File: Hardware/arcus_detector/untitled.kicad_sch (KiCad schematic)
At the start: 8 parts, among them J3 Arc_Input, U17 MAX11102AUB/V+, U4 MCP662-E/MF, U7 MCP6S91

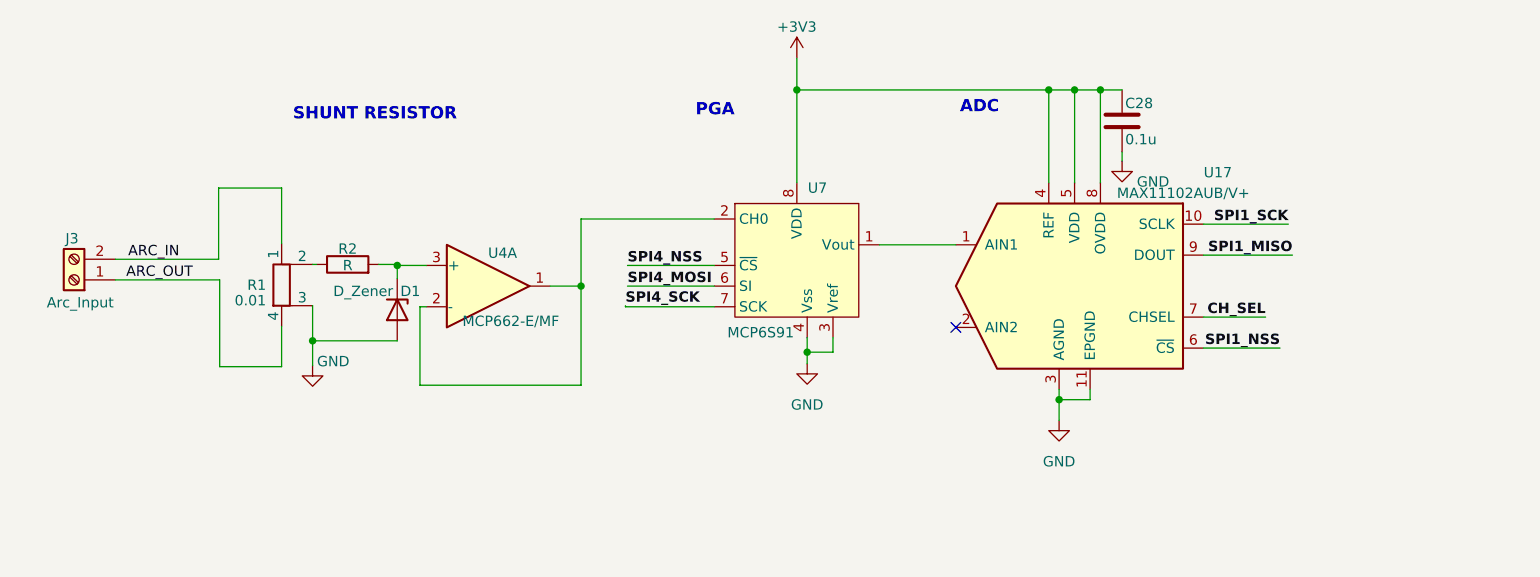
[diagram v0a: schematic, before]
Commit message: - complete sheme of prototype - PGA code works - treshold code added to main
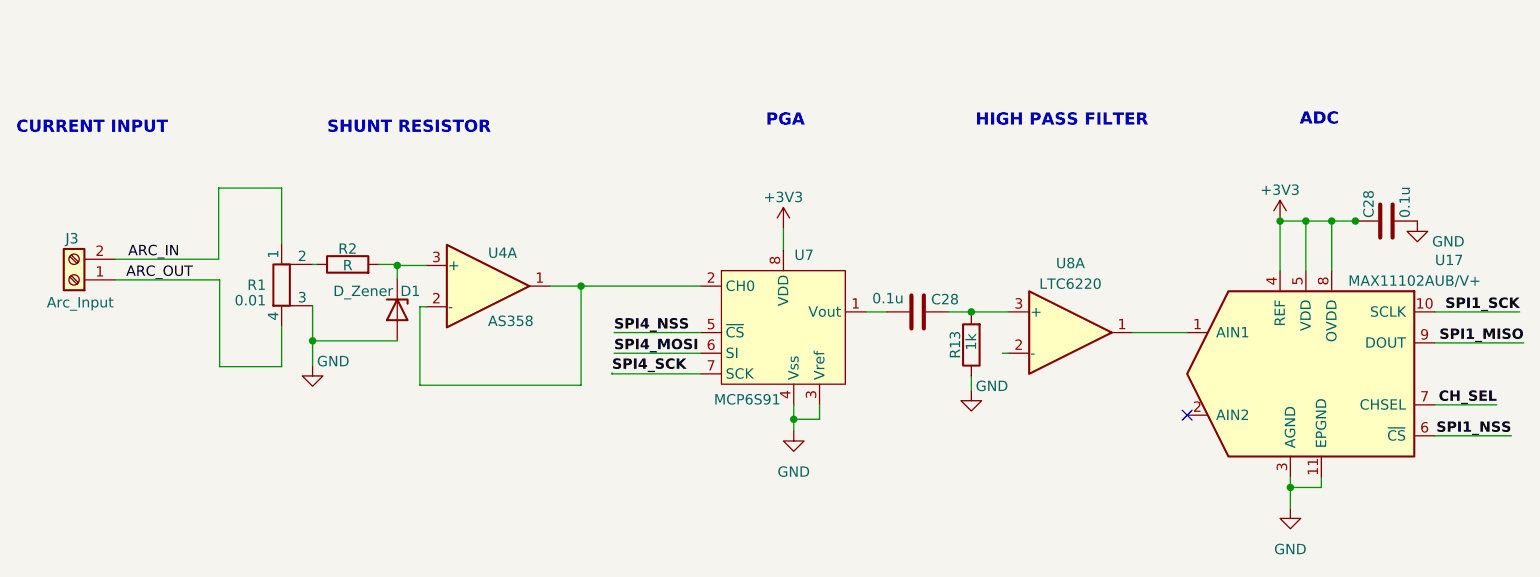
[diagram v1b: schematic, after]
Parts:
- added C28: 0.1u, symbol Device:C
- added R13: 1k, symbol Device:R
- added U8: LTC6220, Package_SO:SOIC-8_3.9x4.9mm_P1.27mm, symbol Amplifier_Operational:MCP6L02x-xSN
- U4: value MCP662-E/MF -> AS358
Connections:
- net GND: now also R13.1
- net at U7.1 (Vout): now also C28.2; no longer U17.1 (AIN1)
- new net: C28.1, R13.2, U8.3 (+)
- new net: U17.1 (AIN1), U8.1
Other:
- note added: "CURRENT INPUT"
- note added: "HIGH PASS FILTER"
- moved on the sheet: C28, U17, U7
